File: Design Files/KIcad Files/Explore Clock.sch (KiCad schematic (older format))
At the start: 19 parts

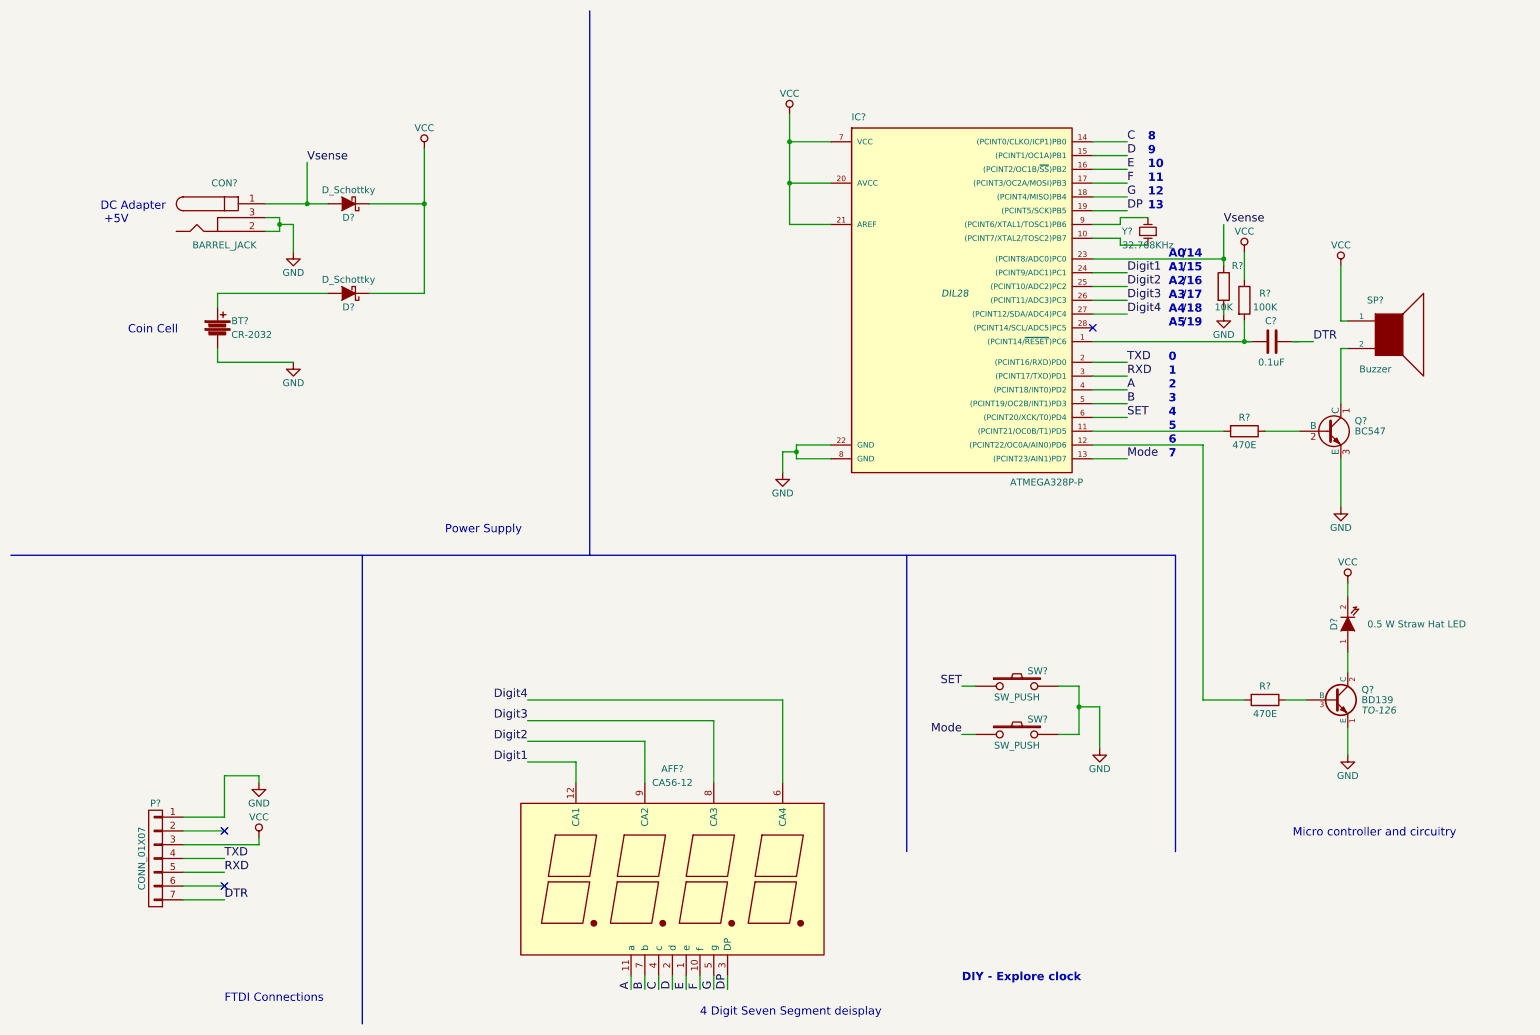
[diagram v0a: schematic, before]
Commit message: Added LDR, Changed Vsense ciruit
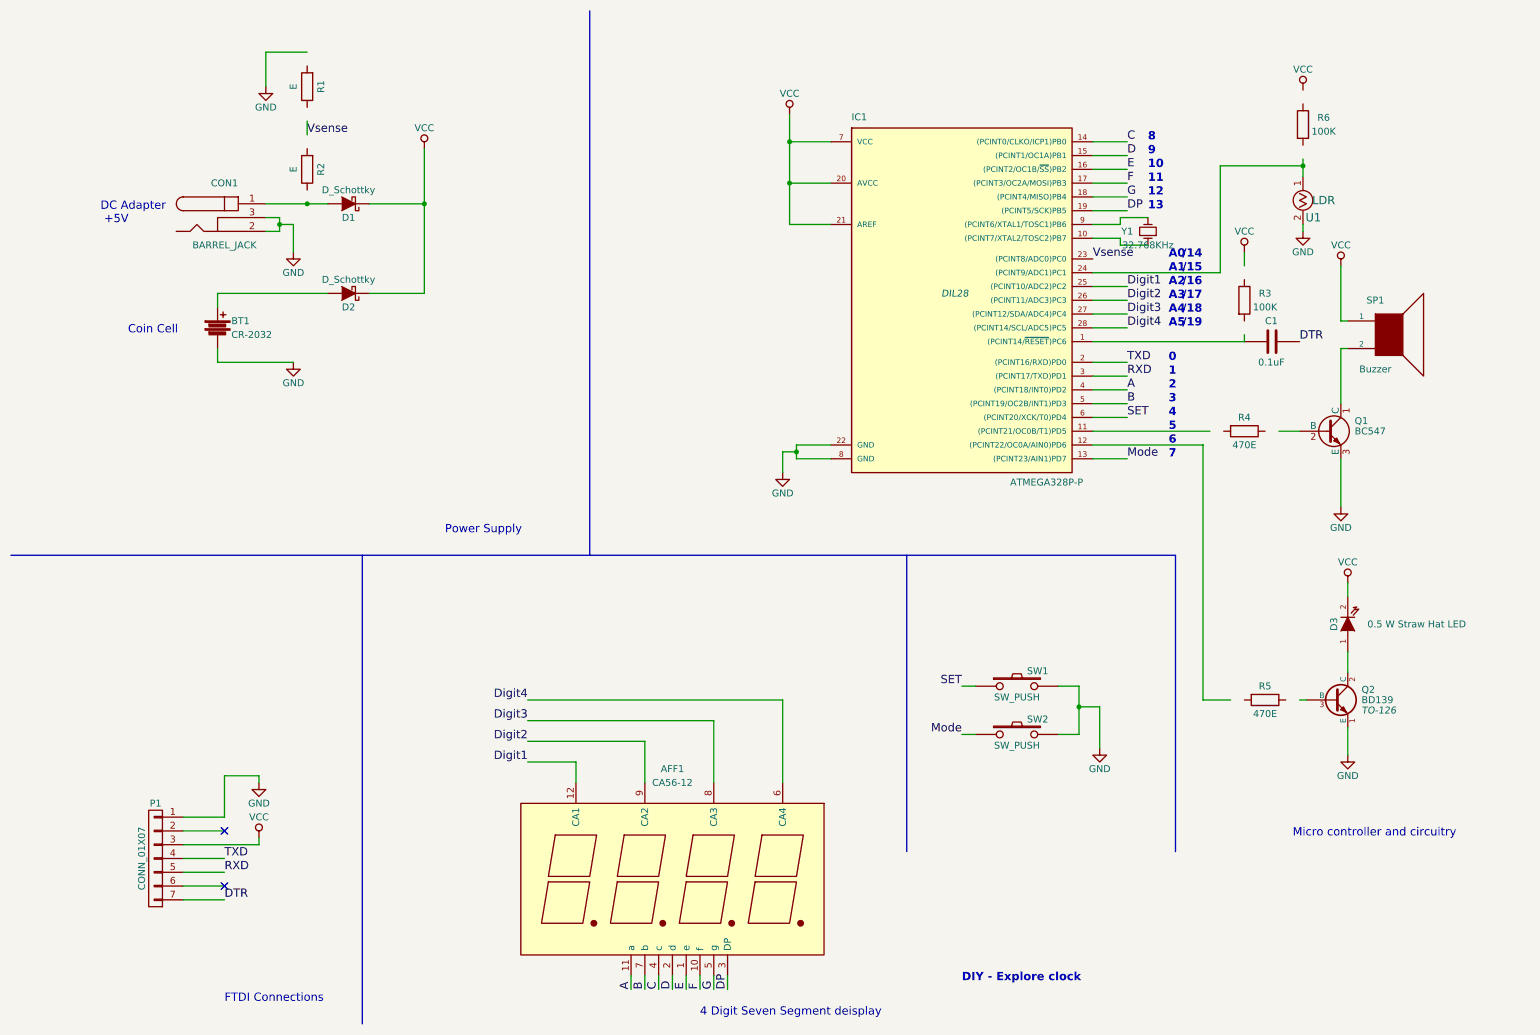
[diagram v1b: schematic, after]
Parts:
- removed R?: 10K, symbol R
- added R1, R2: E, symbol R
- added R6: 100K, symbol R
- added U1: LDR, symbol LDR
- gave numbers to parts that had none: 18
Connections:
- wire segments 100 -> 103
- no-connect marks 3 -> 2

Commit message: 0.5W LED Driving circuit added
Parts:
- removed Q2: BD139, TO-126, symbol BD139
- added Q2: BC547, TO-92, symbol BC547
- added Q3: IRF540N, TO-220, symbol IRF540N
- added R7: 5E/1W, symbol R
- C1: symbol C -> C-RESCUE-Explore_Clock
- D3: symbol LED -> LED-RESCUE-Explore_Clock
- IC1: symbol ATMEGA328P-P -> ATMEGA328P-P-RESCUE-Explore_Clock
- R1, R2, R3, R4, R6: symbol R -> R-RESCUE-Explore_Clock
- R5: value 470E -> 10K; symbol R -> R-RESCUE-Explore_Clock
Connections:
- wire segments 103 -> 109
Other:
- moved on the sheet: R5
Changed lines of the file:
@@
 EESchema Schematic File Version 2
+LIBS:Explore Clock-rescue
 LIBS:power
 LIBS:device
@@
 LIBS:w_opto
 LIBS:led
-LIBS:MCU_BaseBoard-cache
 LIBS:Explore Clock-cache
 EELAYER 25 0
@@
 $EndDescr
 $Comp
-L ATMEGA328P-P IC1
+L ATMEGA328P-P-RESCUE-Explore_Clock IC1
 U 1 1 57EF89E4
 P 7350 2500
@@
 91 D7 3E FA 04 87 BF 7F D8 87 EE E1 C8 9C A2 F7 E4 7B 47 1A 21 A9 E9 AE A6 61 E6 63 11 EF 34 7D
 BD EE 38 A9 51 41 6E 70 71 54 41 3F EC 42 8E BC AB 3D C0 C1 9B A3 8E FF 0F 71 E1 17 88 11 2B 92
-BC 00 00 00 00 49 45 4E 44 AE 42 60 82 39
+BC 00 00 00 00 49 45 4E 44 AE 42 60 82 4C
 EndData
 $EndBitmap
@@
 DIY - Explore clock
 $Comp
-L VCC #PWR01
+L VCC #PWR8
 U 1 1 57EF8CD9
 P 6150 1200
-F 0 "#PWR01" H 6150 1050 50  0001 C CNN
+F 0 "#PWR8" H 6150 1050 50  0001 C CNN
 F 1 "VCC" H 6150 1350 50  0000 C CNN
 F 2 "" H 6150 1200 50  0000 C CNN
@@
 $EndComp
 $Comp
-L GND #PWR02
+L GND #PWR7
 U 1 1 57EF8E24
 P 6100 3800
-F 0 "#PWR02" H 6100 3550 50  0001 C CNN
+F 0 "#PWR7" H 6100 3550 50  0001 C CNN
 F 1 "GND" H 6100 3650 50  0000 C CNN
 F 2 "" H 6100 3800 50  0000 C CNN
@@
 P 8750 2050
 F 0 "Y1" V 8750 2200 50  0000 C CNN
-F 1 "32.768KHz" V 8650 2050 50  0000 C CNN
+F 1 "32.768KHz" V 8750 1750 50  0000 C CNN
 F 2 "" H 8750 2050 50  0000 C CNN
 F 3 "" H 8750 2050 50  0000 C CNN
@@
 $EndComp
 $Comp
-L GND #PWR03
+L GND #PWR4
 U 1 1 57EFA30E
 P 2550 2200
-F 0 "#PWR03" H 2550 1950 50  0001 C CNN
+F 0 "#PWR4" H 2550 1950 50  0001 C CNN
 F 1 "GND" H 2550 2050 50  0000 C CNN
 F 2 "" H 2550 2200 50  0000 C CNN
@@
 $EndComp
 $Comp
-L GND #PWR04
+L GND #PWR5
 U 1 1 57EFA330
 P 2550 3000
-F 0 "#PWR04" H 2550 2750 50  0001 C CNN
+F 0 "#PWR5" H 2550 2750 50  0001 C CNN
 F 1 "GND" H 2550 2850 50  0000 C CNN
 F 2 "" H 2550 3000 50  0000 C CNN
@@
 $EndComp
 $Comp
-L VCC #PWR05
+L VCC #PWR6
 U 1 1 57EFA64B
 P 3500 1450
-F 0 "#PWR05" H 3500 1300 50  0001 C CNN
+F 0 "#PWR6" H 3500 1300 50  0001 C CNN
 F 1 "VCC" H 3500 1600 50  0000 C CNN
 F 2 "" H 3500 1450 50  0000 C CNN
@@
 $EndComp
 $Comp
-L GND #PWR06
+L GND #PWR1
 U 1 1 57EFCEE9
 P 2300 6050
-F 0 "#PWR06" H 2300 5800 50  0001 C CNN
+F 0 "#PWR1" H 2300 5800 50  0001 C CNN
 F 1 "GND" H 2300 5900 50  0000 C CNN
 F 2 "" H 2300 6050 50  0000 C CNN
@@
 NoConn ~ 2050 6400
 $Comp
-L VCC #PWR07
+L VCC #PWR2
 U 1 1 57EFD128
 P 2300 6450
-F 0 "#PWR07" H 2300 6300 50  0001 C CNN
+F 0 "#PWR2" H 2300 6300 50  0001 C CNN
 F 1 "VCC" H 2300 6600 50  0000 C CNN
 F 2 "" H 2300 6450 50  0000 C CNN
@@
 RXD
 $Comp
-L R R3
+L R-RESCUE-Explore_Clock R3
 U 1 1 57EFDF36
 P 9450 2550
@@
 $EndComp
 $Comp
-L C C1
+L C-RESCUE-Explore_Clock C1
 U 1 1 57EFE2B6
 P 9650 2850
@@
 $EndComp
 $Comp
-L R R4
+L R-RESCUE-Explore_Clock R4
 U 1 1 57F0946C
 P 9450 3500
@@
 $EndComp
 $Comp
-L GND #PWR08
+L GND #PWR15
 U 1 1 57F098A3
 P 10150 4050
-F 0 "#PWR08" H 10150 3800 50  0001 C CNN
+F 0 "#PWR15" H 10150 3800 50  0001 C CNN
 F 1 "GND" H 10150 3900 50  0000 C CNN
 F 2 "" H 10150 4050 50  0000 C CNN
@@
 $EndComp
 $Comp
-L VCC #PWR09
+L VCC #PWR14
 U 1 1 57F09B6A
 P 10150 2300
-F 0 "#PWR09" H 10150 2150 50  0001 C CNN
+F 0 "#PWR14" H 10150 2150 50  0001 C CNN
 F 1 "VCC" H 10150 2450 50  0000 C CNN
 F 2 "" H 10150 2300 50  0000 C CNN
@@
 $EndComp
 $Comp
-L BD139 Q2
-U 1 1 57F0B4EA
-P 10100 5450
-F 0 "Q2" H 10300 5525 50  0000 L CNN
-F 1 "BD139" H 10300 5450 50  0000 L CNN
-F 2 "TO-126" H 10300 5375 50  0000 L CIN
-F 3 "" H 10100 5450 50  0000 L CNN
-	1    10100 5450
-	1    0    0    -1
-$EndComp
-$Comp
-L LED D3
+L LED-RESCUE-Explore_Clock D3
 U 1 1 57F0B7AF
 P 10200 4900
@@
 F 3 "" H 10200 4900 50  0000 C CNN
 	1    10200 4900
-	0    -1   -1   0
-$EndComp
-$Comp
-L R R5
+	0    1    1    0
+$EndComp
+$Comp
+L R-RESCUE-Explore_Clock R5
 U 1 1 57F0C815
-P 9600 5450
-F 0 "R5" V 9500 5450 50  0000 C CNN
-F 1 "470E" V 9700 5450 50  0000 C CNN
-F 2 "" V 9530 5450 50  0000 C CNN
-F 3 "" H 9600 5450 50  0000 C CNN
-	1    9600 5450
+P 9500 5500
+F 0 "R5" V 9400 5500 50  0000 C CNN
+F 1 "10K" V 9600 5500 50  0000 C CNN
+F 2 "" V 9430 5500 50  0000 C CNN
+F 3 "" H 9500 5500 50  0000 C CNN
+	1    9500 5500
 	0    1    1    0
 $EndComp
 $Comp
-L VCC #PWR010
+L VCC #PWR16
 U 1 1 57F0D12E
 P 10200 4600
-F 0 "#PWR010" H 10200 4450 50  0001 C CNN
+F 0 "#PWR16" H 10200 4450 50  0001 C CNN
 F 1 "VCC" H 10200 4750 50  0000 C CNN
 F 2 "" H 10200 4600 50  0000 C CNN
 F 3 "" H 10200 4600 50  0000 C CNN
 	1    10200 4600
-	1    0    0    -1
-$EndComp
-$Comp
-L GND #PWR011
-U 1 1 57F0D65B
-P 10200 5850
-F 0 "#PWR011" H 10200 5600 50  0001 C CNN
-F 1 "GND" H 10200 5700 50  0000 C CNN
-F 2 "" H 10200 5850 50  0000 C CNN
-F 3 "" H 10200 5850 50  0000 C CNN
-	1    10200 5850
 	1    0    0    -1
 $EndComp
@@
 $EndComp
 $Comp
-L GND #PWR012
+L GND #PWR9
 U 1 1 57F1136E
 P 8400 5800
-F 0 "#PWR012" H 8400 5550 50  0001 C CNN
+F 0 "#PWR9" H 8400 5550 50  0001 C CNN
 F 1 "GND" H 8400 5650 50  0000 C CNN
 F 2 "" H 8400 5800 50  0000 C CNN
@@
 Text Notes 5500 7750 0    60   ~ 0
 4 Digit Seven Segment deisplay
-Text Notes 9800 6450 0    60   ~ 0
+Text Notes 5000 4300 0    50   ~ 0
 Micro controller and circuitry
 $Comp
-L VCC #PWR013
+L VCC #PWR10
 U 1 1 57F1B754
 P 9450 2200
-F 0 "#PWR013" H 9450 2050 50  0001 C CNN
+F 0 "#PWR10" H 9450 2050 50  0001 C CNN
 F 1 "VCC" H 9450 2350 50  0000 C CNN
 F 2 "" H 9450 2200 50  0000 C CNN
@@
 	1    0    0    -1
 $EndComp
-Text Label 8350 2250 0    60   ~ 0
+Text Label 8550 2250 0    60   ~ 0
 Vsense
-Text Label 2650 1350 0    60   ~ 0
+Text Label 2850 1300 0    60   ~ 0
 Vsense
 Wire Wire Line
@@
 	10200 5250 10200 5100
 Wire Wire Line
-	8350 3600 9150 3600
-Wire Wire Line
-	9150 3600 9150 5450
+	8350 3600 9200 3600
 Wire Wire Line
 	10200 4600 10200 4700
-Wire Wire Line
-	10200 5650 10200 5850
 Wire Wire Line
 	8100 5350 8250 5350
@@
 	8950 4400 8950 6550
 $Comp
-L R R2
+L R-RESCUE-Explore_Clock R2
 U 1 1 57F34619
 P 2650 1600
@@
 $EndComp
 $Comp
-L R R1
+L R-RESCUE-Explore_Clock R1
 U 1 1 57F348A8
 P 2650 1000
@@
 	2650 1350 2650 1250
 $Comp
-L GND #PWR014
+L GND #PWR3
 U 1 1 57F34AB2
 P 2350 1000
-F 0 "#PWR014" H 2350 750 50  0001 C CNN
+F 0 "#PWR3" H 2350 750 50  0001 C CNN
 F 1 "GND" H 2350 850 50  0000 C CNN
 F 2 "" H 2350 1000 50  0000 C CNN
@@
 	8350 2750 8600 2750
 $Comp
-L R R6
+L R-RESCUE-Explore_Clock R6
 U 1 1 57F35736
 P 9875 1275
@@
 $EndComp
 $Comp
-L VCC #PWR015
+L VCC #PWR12
 U 1 1 57F35B1B
 P 9875 1025
-F 0 "#PWR015" H 9875 875 50  0001 C CNN
+F 0 "#PWR12" H 9875 875 50  0001 C CNN
 F 1 "VCC" H 9875 1175 50  0000 C CNN
 F 2 "" H 9875 1025 50  0000 C CNN
@@
 $EndComp
 $Comp
-L GND #PWR016
+L GND #PWR13
 U 1 1 57F35D0A
 P 9875 2050
-F 0 "#PWR016" H 9875 1800 50  0001 C CNN
+F 0 "#PWR13" H 9875 1800 50  0001 C CNN
 F 1 "GND" H 9875 1900 50  0000 C CNN
 F 2 "" H 9875 2050 50  0000 C CNN
@@
 Wire Wire Line
 	9200 3500 8350 3500
-Wire Wire Line
-	9850 5450 9900 5450
-Wire Wire Line
-	9150 5450 9350 5450
+$Comp
+L IRF540N Q3
+U 1 1 57F36D74
+P 10100 5450
+F 0 "Q3" H 10350 5525 50  0000 L CNN
+F 1 "IRF540N" H 10350 5450 50  0000 L CNN
+F 2 "TO-220" H 10350 5375 50  0000 L CIN
+F 3 "" H 10100 5450 50  0000 L CNN
+	1    10100 5450
+	1    0    0    -1
+$EndComp
+$Comp
+L BC547 Q2
+U 1 1 57F36F93
+P 9950 5950
+F 0 "Q2" H 10150 6025 50  0000 L CNN
+F 1 "BC547" H 10150 5950 50  0000 L CNN
+F 2 "TO-92" H 10150 5875 50  0000 L CIN
+F 3 "" H 9950 5950 50  0000 L CNN
+	1    9950 5950
+	-1   0    0    -1
+$EndComp
+Wire Wire Line
+	9750 5500 9900 5500
+Wire Wire Line
+	9250 5500 9200 5500
+Wire Wire Line
+	9200 5500 9200 3600
+$Comp
+L R R7
+U 1 1 57F39D42
+P 10200 6200
+F 0 "R7" H 10300 6150 50  0000 C CNN
+F 1 "5E/1W" H 10400 6250 50  0000 C CNN
+F 2 "" V 10130 6200 50  0000 C CNN
+F 3 "" H 10200 6200 50  0000 C CNN
+	1    10200 6200
+	1    0    0    -1
+$EndComp
+Wire Wire Line
+	10200 5650 10200 6050
+$Comp
+L GND #PWR11
+U 1 1 57F3A574
+P 9850 6350
+F 0 "#PWR11" H 9850 6100 50  0001 C CNN
+F 1 "GND" H 9850 6200 50  0000 C CNN
+F 2 "" H 9850 6350 50  0000 C CNN
+F 3 "" H 9850 6350 50  0000 C CNN
+	1    9850 6350
+	1    0    0    -1
+$EndComp
+Wire Wire Line
+	9850 6150 9850 6350
+Wire Wire Line
+	10150 5950 10200 5950
+Connection ~ 10200 5950
+$Comp
+L GND #PWR17
+U 1 1 57F3C1E0
+P 10200 6400
+F 0 "#PWR17" H 10200 6150 50  0001 C CNN
+F 1 "GND" H 10350 6300 50  0000 C CNN
+F 2 "" H 10200 6400 50  0000 C CNN
+F 3 "" H 10200 6400 50  0000 C CNN
+	1    10200 6400
+	1    0    0    -1
+$EndComp
+Wire Wire Line
+	10200 6400 10200 6350
+Wire Wire Line
+	9850 5750 9850 5500
+Connection ~ 9850 5500
+Wire Wire Line
+	2650 1300 2850 1300
+Connection ~ 2650 1300
+Wire Wire Line
+	8550 2250 8350 2250
 $EndSCHEMATC

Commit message: Power LED added
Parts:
- added D?: Power LED, symbol LED-RESCUE-Explore_Clock
- added R?: 1K, symbol R-RESCUE-Explore_Clock
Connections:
- net GND: now also R?.2
- net at CON1.1, D1.2 (A), R2.1: now also D?.1 (A)
- new net: D?.2 (K), R?.1
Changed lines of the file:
@@
 91 D7 3E FA 04 87 BF 7F D8 87 EE E1 C8 9C A2 F7 E4 7B 47 1A 21 A9 E9 AE A6 61 E6 63 11 EF 34 7D
 BD EE 38 A9 51 41 6E 70 71 54 41 3F EC 42 8E BC AB 3D C0 C1 9B A3 8E FF 0F 71 E1 17 88 11 2B 92
-BC 00 00 00 00 49 45 4E 44 AE 42 60 82 4C
+BC 00 00 00 00 49 45 4E 44 AE 42 60 82 6A
 EndData
 $EndBitmap
@@
 L GND #PWR3
 U 1 1 57F34AB2
-P 2350 1000
-F 0 "#PWR3" H 2350 750 50  0001 C CNN
-F 1 "GND" H 2350 850 50  0000 C CNN
-F 2 "" H 2350 1000 50  0000 C CNN
-F 3 "" H 2350 1000 50  0000 C CNN
-	1    2350 1000
-	1    0    0    -1
-$EndComp
-Wire Wire Line
-	2350 1000 2350 750
-Wire Wire Line
-	2350 750  2650 750
+P 3000 650
+F 0 "#PWR3" H 3000 400 50  0001 C CNN
+F 1 "GND" H 3000 500 50  0000 C CNN
+F 2 "" H 3000 650 50  0000 C CNN
+F 3 "" H 3000 650 50  0000 C CNN
+	1    3000 650
+	1    0    0    -1
+$EndComp
 Wire Wire Line
 	8350 2750 8600 2750
@@
 Wire Wire Line
 	8550 2250 8350 2250
+$Comp
+L LED-RESCUE-Explore_Clock D?
+U 1 1 57F63B9E
+P 2450 1550
+F 0 "D?" H 2450 1650 50  0000 C CNN
+F 1 "Power LED" V 2600 1900 50  0000 C CNN
+F 2 "" H 2450 1550 50  0000 C CNN
+F 3 "" H 2450 1550 50  0000 C CNN
+	1    2450 1550
+	0    -1   -1   0
+$EndComp
+Wire Wire Line
+	2650 750  2650 600
+Wire Wire Line
+	2450 600  3000 600
+Wire Wire Line
+	3000 600  3000 650
+$Comp
+L R-RESCUE-Explore_Clock R?
+U 1 1 57F64304
+P 2450 950
+F 0 "R?" V 2350 950 50  0000 C CNN
+F 1 "1K" V 2550 950 50  0000 C CNN
+F 2 "" V 2380 950 50  0000 C CNN
+F 3 "" H 2450 950 50  0000 C CNN
+	1    2450 950
+	-1   0    0    1
+$EndComp
+Wire Wire Line
+	2450 1750 2450 1850
+Connection ~ 2450 1850
+Wire Wire Line
+	2450 1350 2450 1200
+Wire Wire Line
+	2450 700  2450 600
+Connection ~ 2650 600
 $EndSCHEMATC
